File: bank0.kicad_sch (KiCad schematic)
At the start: 16 parts, among them U1 xc7z010clg400, U3 W25Q256FVEI

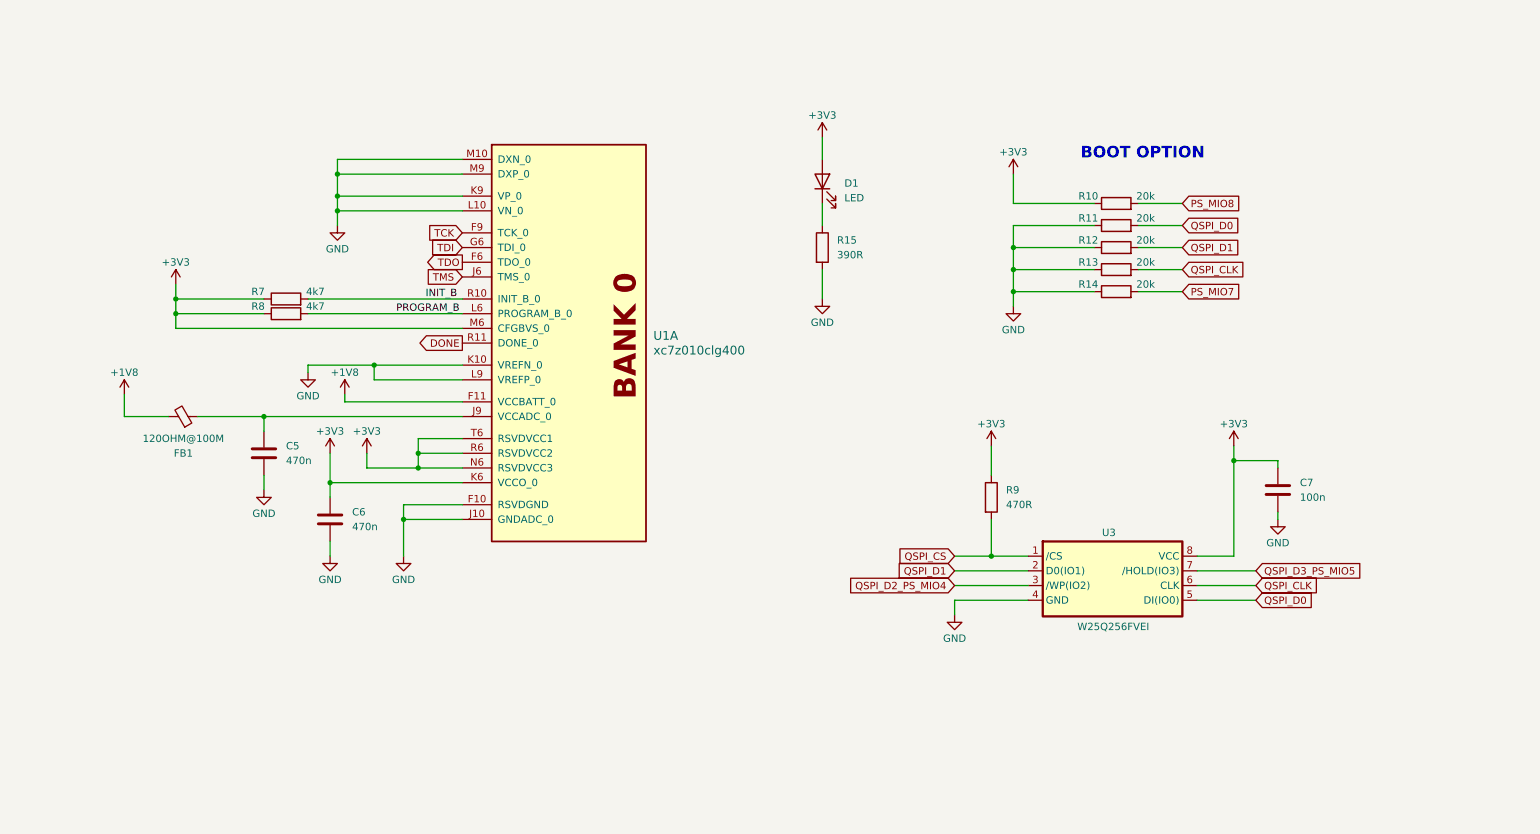
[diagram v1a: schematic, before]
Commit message: feat: finish ddr3 sch design
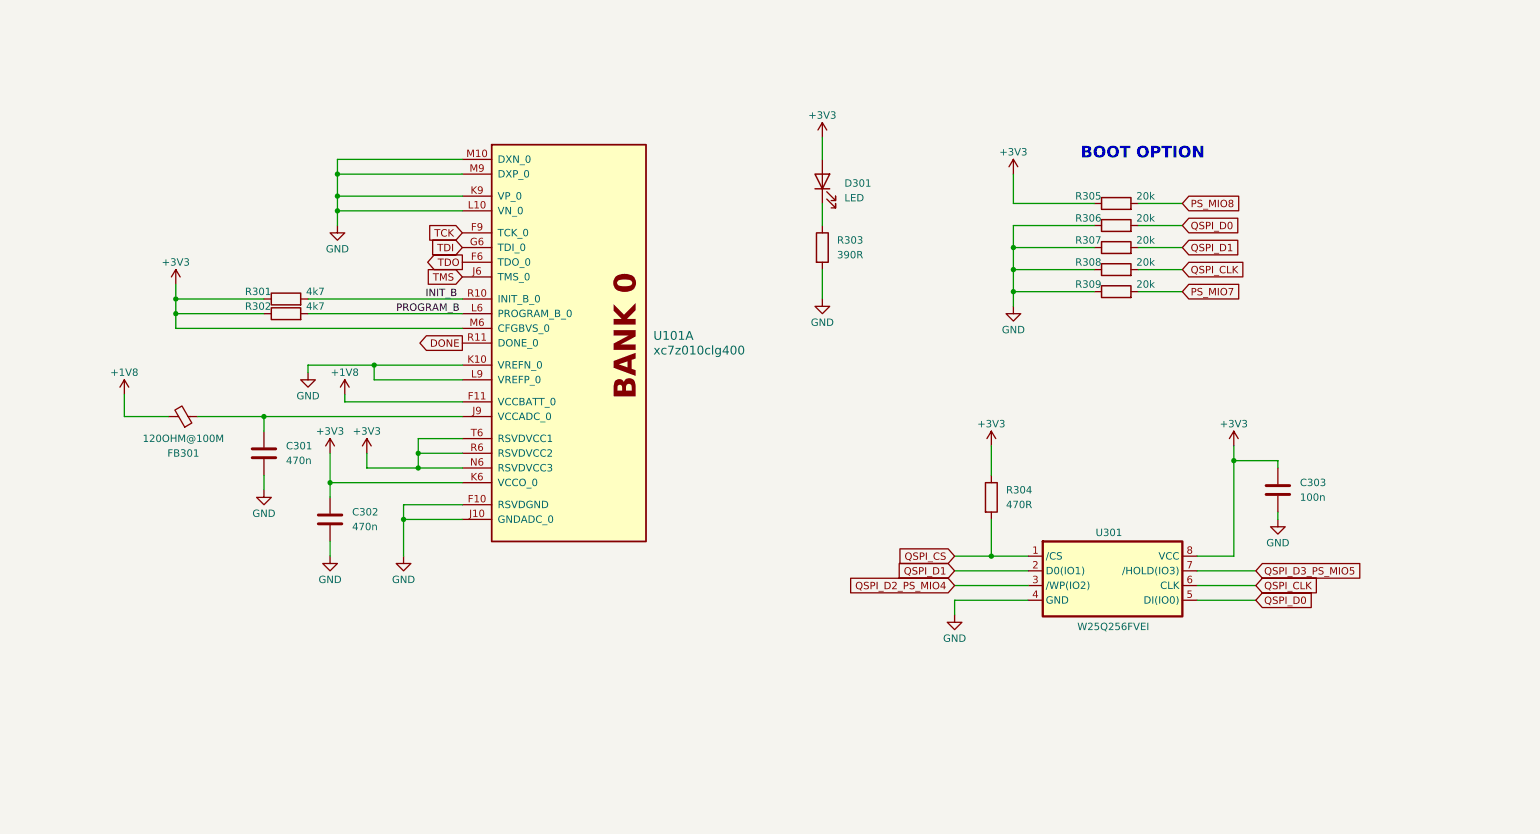
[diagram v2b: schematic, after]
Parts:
- U301: renamed from U3; footprint (none) -> Footprints:IC_W25N04KVZEIU
- renumbered C5 to C301, C6 to C302, C7 to C303, D1 to D301, FB1 to FB301, R7 to R301, R8 to R302, R15 to R303, R9 to R304, R10 to R305, R11 to R306, R12 to R307, R13 to R308, R14 to R309, U1 to U101

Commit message: feat: start to routing DDR3
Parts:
- U101: footprint (none) -> Package_BGA:Xilinx_CLG400
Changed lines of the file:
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@@
 			)
 		)
-		(property "Footprint" ""
+		(property "Footprint" "Package_BGA:Xilinx_CLG400"
 			(at 36.83 41.91 0)
 			(hide yes)

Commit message: feat: restart routing ddr
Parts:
- C303: footprint (none) -> Capacitor_SMD:C_0402_1005Metric
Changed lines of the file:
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@@
 			)
 		)
-		(property "Footprint" ""
+		(property "Footprint" "Capacitor_SMD:C_0402_1005Metric"
 			(at 237.1852 113.03 0)
 			(hide yes)

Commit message: feat: continue routing ddr
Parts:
- removed D301: LED, symbol Device:LED
- removed R303: 390R, symbol Device:R
- added D302: LED, symbol Device:LED
- added J301: Conn_01x04_Pin, symbol Connector:Conn_01x04_Pin
- added R310, R311, R312, R313: 20k, symbol Device:R
- added R314: 390R, symbol Device:R
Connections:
- net +3V3: now also D302.2 (A), J301.4 (Pin_4), R310.1
- net GND: now also J301.2 (Pin_2), R313.1, R314.2
- net QSPI_D2_PS_MIO4: now also R312.1
- net QSPI_D3_PS_MIO5: now also R311.1
- new net: J301.3 (Pin_3), R312.2, R313.2
- new net: D302.1 (K), R314.1
- new net: J301.1 (Pin_1), R310.2, R311.2
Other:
- moved on the sheet: C301, C302, C303, FB301, R301, R302, R304, R305, R306, R307, R308, R309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

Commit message: feat: continue sch design
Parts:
- added D303: LED, symbol Device:LED
- added J302: Conn_02x05_Odd_Even, symbol Connector_Generic:Conn_02x05_Odd_Even
- added Q301: MMBT3904, Package_TO_SOT_SMD:SOT-23, symbol Transistor_BJT:MMBT3904
- added R315: 330R, symbol Device:R
- added R316, R317: 1k, symbol Device:R
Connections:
- net +3V3: now also J302.1 (Pin_1), J302.2 (Pin_2), R315.1
- net DONE: now also D303.2 (A), R315.2
- net GND: now also J302.10 (Pin_10), J302.8 (Pin_8), J302.9 (Pin_9), Q301.2 (E)
- net TCK: now also J302.4 (Pin_4)
- net TDI: now also J302.6 (Pin_6)
- net TDO: now also J302.5 (Pin_5)
- net TMS: now also J302.3 (Pin_3)
- new net: D303.1 (K), R316.1
- new net: Q301.3 (C), R316.2
- new net: Q301.1 (B), R317.2
- new net +1V5: R317.1
- new net nTRST: J302.7 (Pin_7)
- no-connect marks 0 -> 1

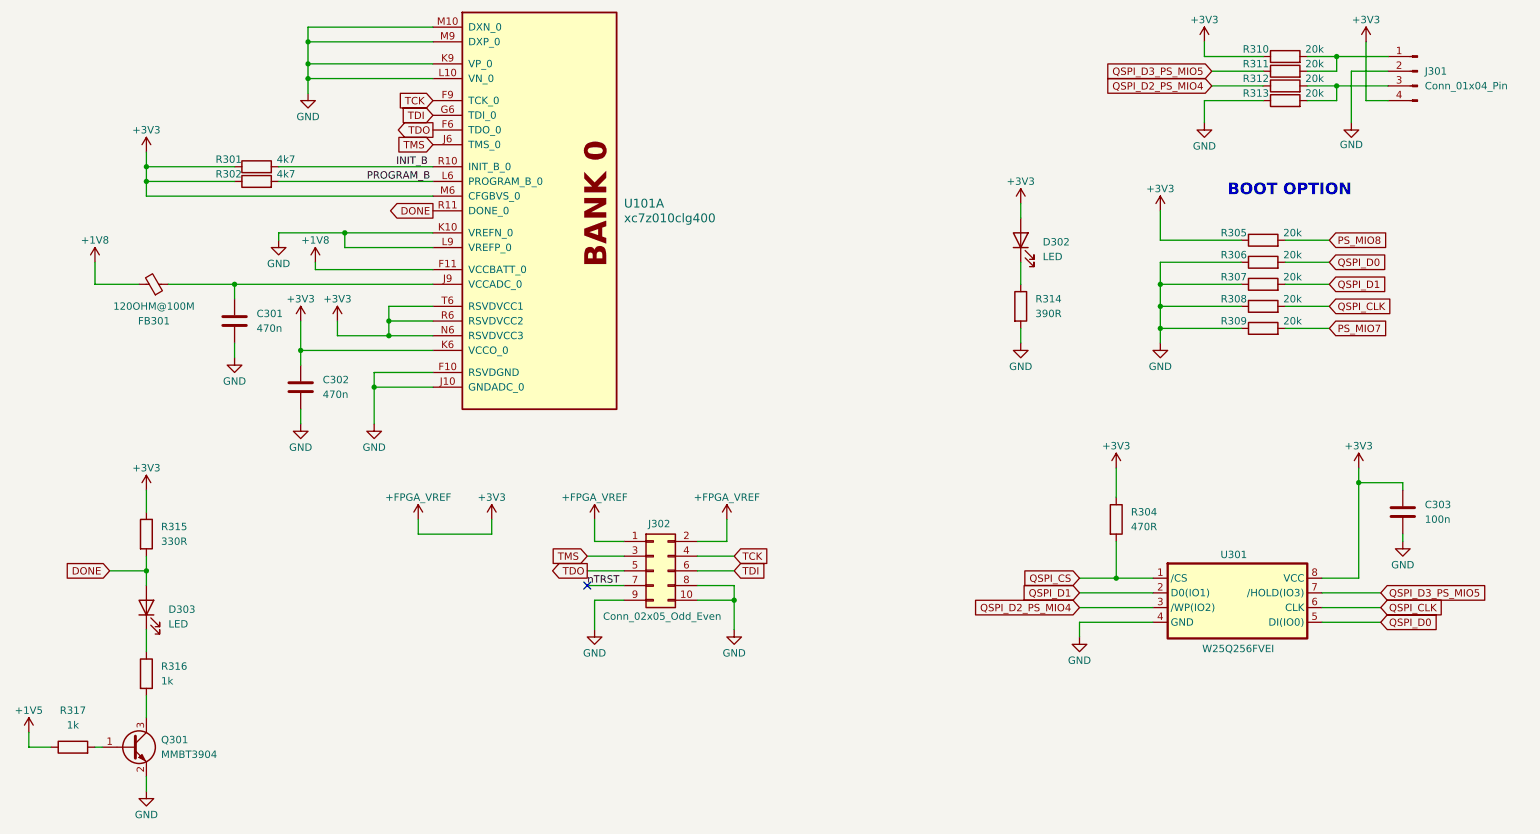
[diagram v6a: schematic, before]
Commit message: feat: continue routing ddr3
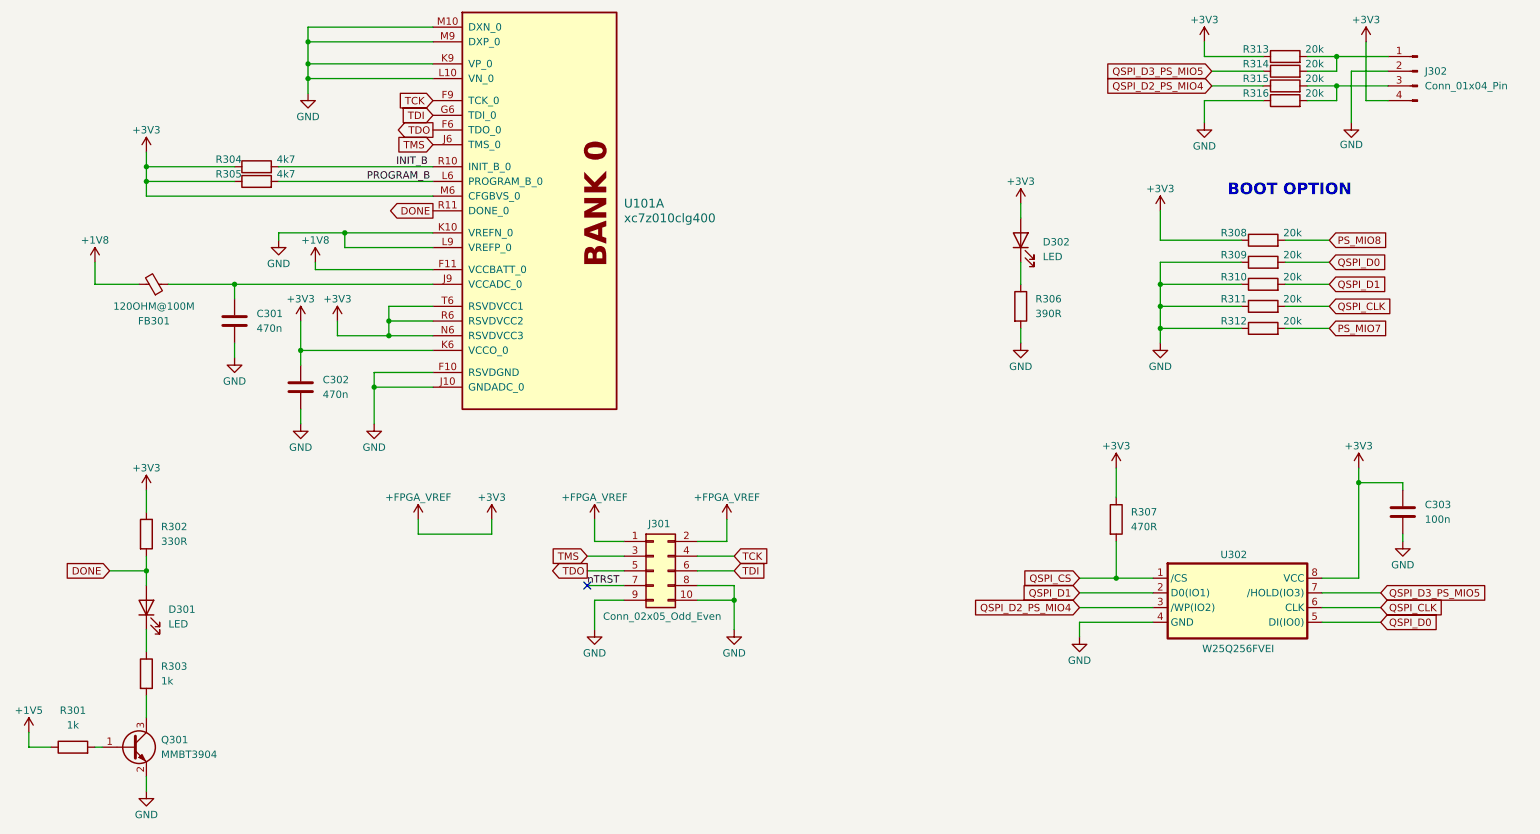
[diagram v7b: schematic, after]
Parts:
- C301, C302: footprint (none) -> Capacitor_SMD:C_0402_1005Metric
- renumbered D303 to D301, J302 to J301, J301 to J302, R317 to R301, R315 to R302, R316 to R303, R301 to R304, R302 to R305, R314 to R306, R304 to R307, R305 to R308, R306 to R309, R307 to R310, R308 to R311, R309 to R312, R310 to R313, R311 to R314, R312 to R315, R313 to R316, U301 to U302

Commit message: feat: continue routing
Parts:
- D301, D302: footprint (none) -> LED_SMD:LED_0603_1608Metric
- R301, R302, R303, R304, R305, R306, R307, R308, R309, R310, R311, R312, R313, R314, R315, R316: footprint (none) -> Resistor_SMD:R_0402_1005Metric
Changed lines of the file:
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@@
 			)
 		)
-		(property "Footprint" ""
+		(property "Footprint" "Resistor_SMD:R_0402_1005Metric"
 			(at 38.862 140.97 90)
 			(hide yes)
@@
 			)
 		)
-		(property "Footprint" ""
+		(property "Footprint" "Resistor_SMD:R_0402_1005Metric"
 			(at 237.49 43.688 90)
 			(hide yes)
@@
 			)
 		)
-		(property "Footprint" ""
+		(property "Footprint" "LED_SMD:LED_0603_1608Metric"
 			(at 191.77 66.04 0)
 			(hide yes)
@@
 			)
 		)
-		(property "Footprint" ""
+		(property "Footprint" "Resistor_SMD:R_0402_1005Metric"
 			(at 233.68 71.628 90)
 			(hide yes)
@@
 			)
 		)
-		(property "Footprint" ""
+		(property "Footprint" "Resistor_SMD:R_0402_1005Metric"
 			(at 27.94 155.448 90)
 			(hide yes)
@@
 			)
 		)
-		(property "Footprint" ""
+		(property "Footprint" "Resistor_SMD:R_0402_1005Metric"
 			(at 233.68 75.438 90)
 			(hide yes)
@@
 			)
 		)
-		(property "Footprint" ""
+		(property "Footprint" "LED_SMD:LED_0603_1608Metric"
 			(at 40.64 129.54 0)
 			(hide yes)
@@
 			)
 		)
-		(property "Footprint" ""
+		(property "Footprint" "Resistor_SMD:R_0402_1005Metric"
 			(at 237.49 41.148 90)
 			(hide yes)
@@
 			)
 		)
-		(property "Footprint" ""
+		(property "Footprint" "Resistor_SMD:R_0402_1005Metric"
 			(at 233.68 83.058 90)
 			(hide yes)
@@
 			)
 		)
-		(property "Footprint" ""
+		(property "Footprint" "Resistor_SMD:R_0402_1005Metric"
 			(at 237.49 36.068 90)
 			(hide yes)
@@
 			)
 		)
-		(property "Footprint" ""
+		(property "Footprint" "Resistor_SMD:R_0402_1005Metric"
 			(at 233.68 67.818 90)
 			(hide yes)
@@
 			)
 		)
-		(property "Footprint" ""
+		(property "Footprint" "Resistor_SMD:R_0402_1005Metric"
 			(at 189.992 77.47 90)
 			(hide yes)
@@
 			)
 		)
-		(property "Footprint" ""
+		(property "Footprint" "Resistor_SMD:R_0402_1005Metric"
 			(at 237.49 38.608 90)
 			(hide yes)
@@
 			)
 		)
-		(property "Footprint" ""
+		(property "Footprint" "Resistor_SMD:R_0402_1005Metric"
 			(at 59.69 57.658 90)
 			(hide yes)
@@
 			)
 		)
-		(property "Footprint" ""
+		(property "Footprint" "Resistor_SMD:R_0402_1005Metric"
 			(at 233.68 79.248 90)
 			(hide yes)
@@
 			)
 		)
-		(property "Footprint" ""
+		(property "Footprint" "Resistor_SMD:R_0402_1005Metric"
 			(at 38.862 116.84 90)
 			(hide yes)
@@
 			)
 		)
-		(property "Footprint" ""
+		(property "Footprint" "Resistor_SMD:R_0402_1005Metric"
 			(at 206.502 114.3 90)
 			(hide yes)
@@
 			)
 		)
-		(property "Footprint" ""
+		(property "Footprint" "Resistor_SMD:R_0402_1005Metric"
 			(at 59.69 55.118 90)
 			(hide yes)
